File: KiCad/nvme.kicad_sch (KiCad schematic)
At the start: 35 parts, among them J10 Bus_M.2_Socket_M, J11 Bus_M.2_Socket_M, J12 Bus_M.2_Socket_M, J13 Bus_M.2_Socket_M, J14 Bus_M.2_Socket_M

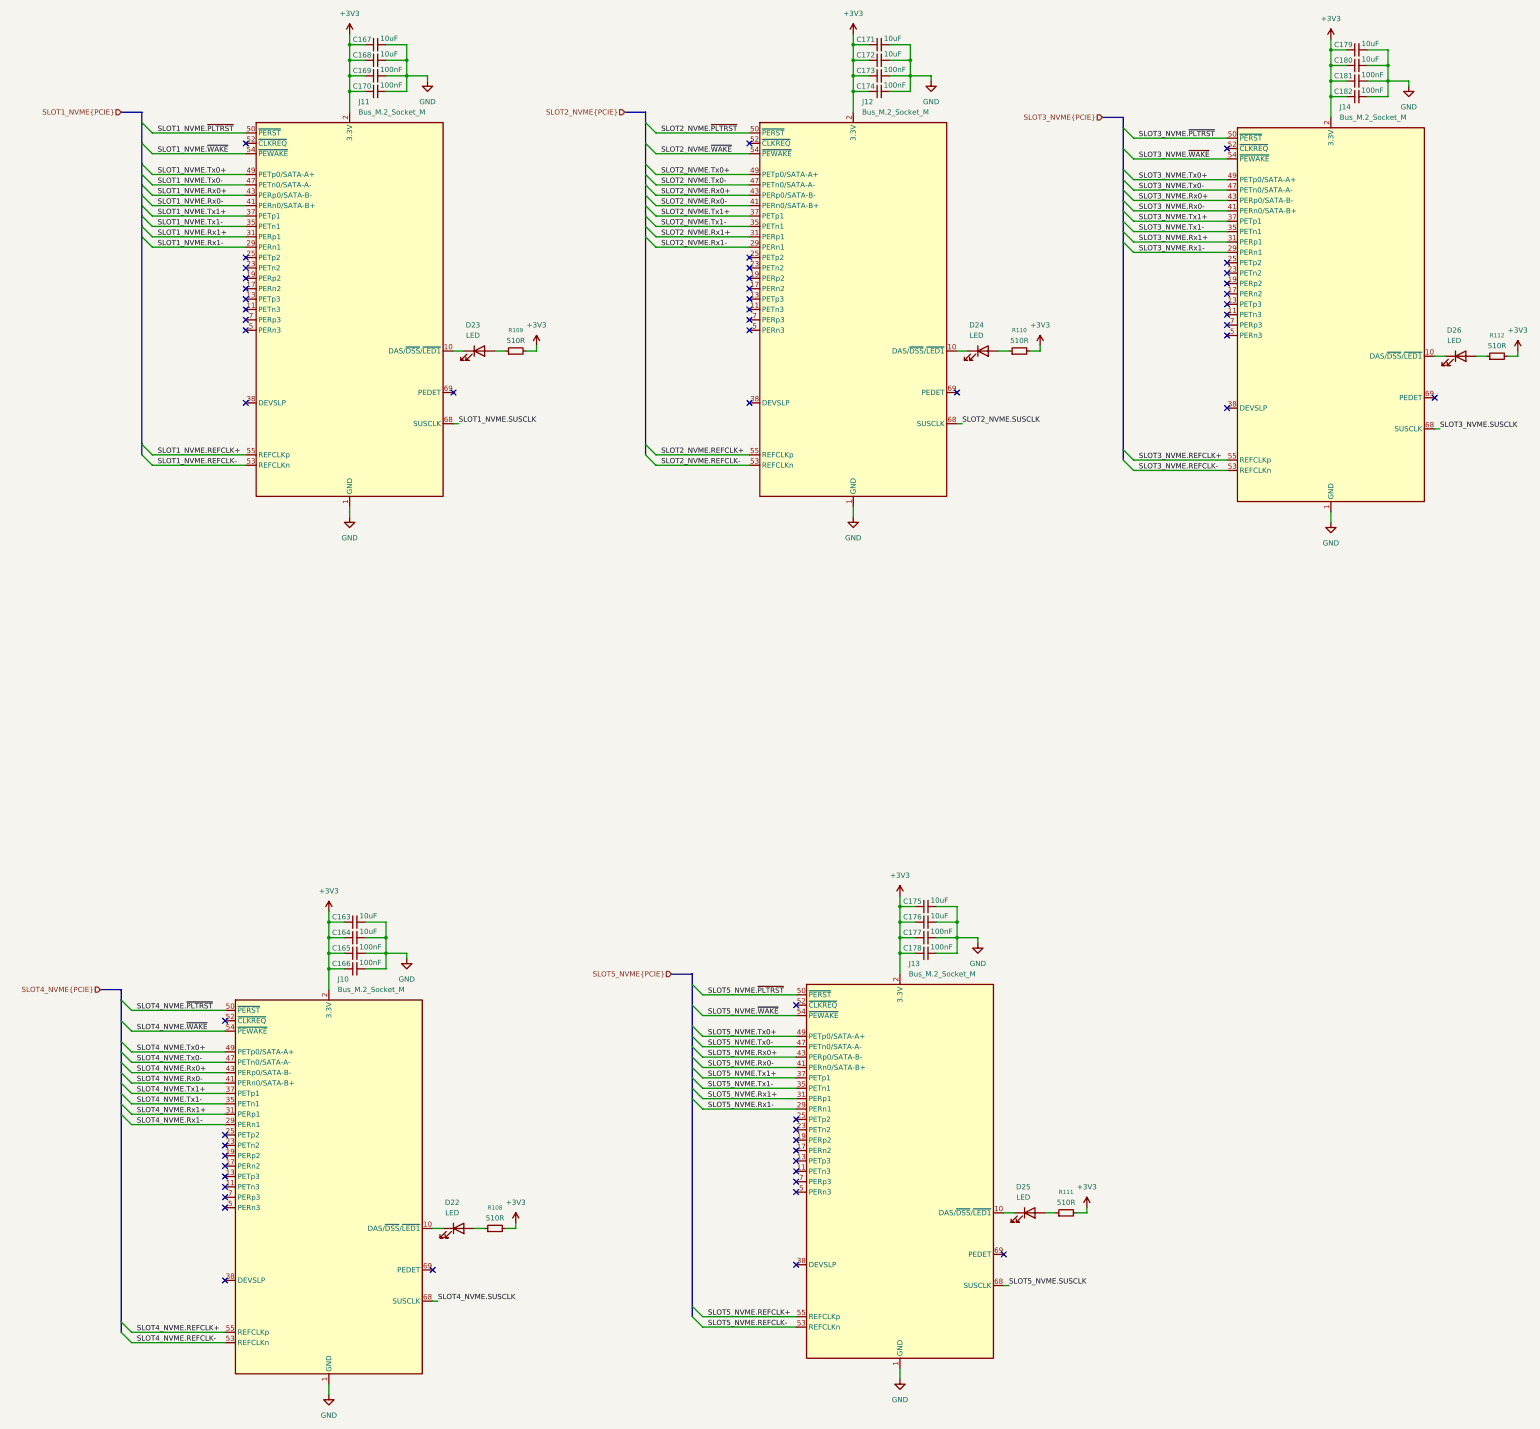
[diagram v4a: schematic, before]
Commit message: Lots of tiny capacitors
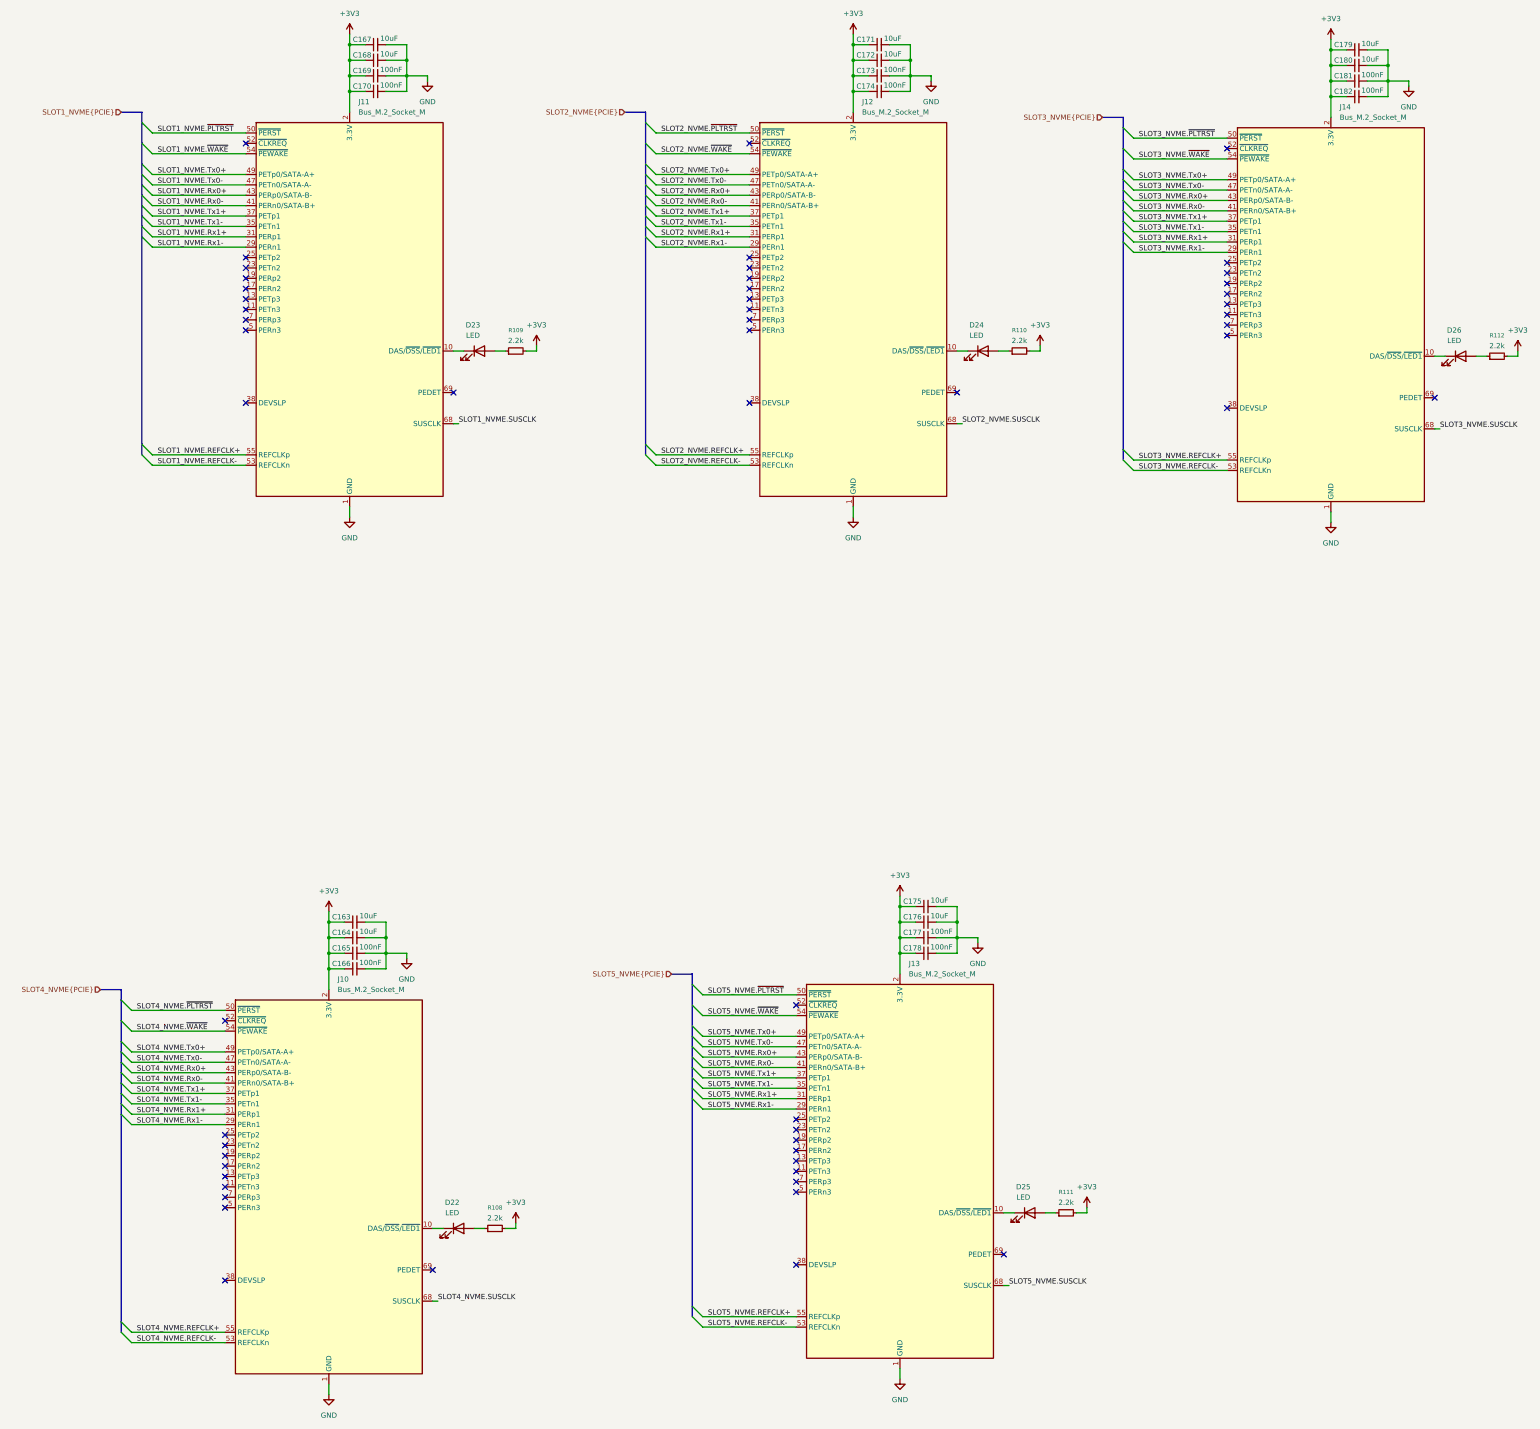
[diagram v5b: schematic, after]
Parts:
- C165, C166, C169, C170, C173, C174, C177, C178, C181, C182: footprint Capacitor_SMD:C_0603_1608Metric -> Capacitor_SMD:C_0402_1005Metric
- R108, R109, R110, R111, R112: value 510R -> 2.2k; footprint (none) -> Resistor_SMD:R_0402_1005Metric
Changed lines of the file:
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@@
 			)
 		)
-		(property "Footprint" "Capacitor_SMD:C_0603_1608Metric"
+		(property "Footprint" "Capacitor_SMD:C_0402_1005Metric"
 			(at 298.45 259.08 0)
 			(effects
@@
 			)
 		)
-		(property "Footprint" "Capacitor_SMD:C_0603_1608Metric"
+		(property "Footprint" "Capacitor_SMD:C_0402_1005Metric"
 			(at 158.75 259.08 0)
 			(effects
@@
 			)
 		)
-		(property "Footprint" "Capacitor_SMD:C_0603_1608Metric"
+		(property "Footprint" "Capacitor_SMD:C_0402_1005Metric"
 			(at 287.02 48.26 0)
 			(effects
@@
 			)
 		)
-		(property "Value" "510R"
+		(property "Value" "2.2k"
 			(at 198.12 109.22 90)
 			(effects
@@
 			)
 		)
-		(property "Footprint" ""
+		(property "Footprint" "Resistor_SMD:R_0402_1005Metric"
 			(at 198.12 111.76 0)
 			(effects
@@
 			)
 		)
-		(property "Value" "510R"
+		(property "Value" "2.2k"
 			(at 193.04 323.85 90)
 			(effects
@@
 			)
 		)
-		(property "Footprint" ""
+		(property "Footprint" "Resistor_SMD:R_0402_1005Metric"
 			(at 193.04 326.39 0)
 			(effects
@@
 			)
 		)
-		(property "Footprint" "Capacitor_SMD:C_0603_1608Metric"
+		(property "Footprint" "Capacitor_SMD:C_0402_1005Metric"
 			(at 163.83 48.26 0)
 			(effects
@@
 			)
 		)
-		(property "Value" "510R"
+		(property "Value" "2.2k"
 			(at 321.31 109.22 90)
 			(effects
@@
 			)
 		)
-		(property "Footprint" ""
+		(property "Footprint" "Resistor_SMD:R_0402_1005Metric"
 			(at 321.31 111.76 0)
 			(effects
@@
 			)
 		)
-		(property "Footprint" "Capacitor_SMD:C_0603_1608Metric"
+		(property "Footprint" "Capacitor_SMD:C_0402_1005Metric"
 			(at 298.45 255.27 0)
 			(effects
@@
 			)
 		)
-		(property "Footprint" "Capacitor_SMD:C_0603_1608Metric"
+		(property "Footprint" "Capacitor_SMD:C_0402_1005Metric"
 			(at 163.83 44.45 0)
 			(effects
@@
 			)
 		)
-		(property "Footprint" "Capacitor_SMD:C_0603_1608Metric"
+		(property "Footprint" "Capacitor_SMD:C_0402_1005Metric"
 			(at 287.02 44.45 0)
 			(effects
@@
 			)
 		)
-		(property "Value" "510R"
+		(property "Value" "2.2k"
 			(at 438.15 110.49 90)
 			(effects
@@
 			)
 		)
-		(property "Footprint" ""
+		(property "Footprint" "Resistor_SMD:R_0402_1005Metric"
 			(at 438.15 113.03 0)
 			(effects
@@
 			)
 		)
-		(property "Footprint" "Capacitor_SMD:C_0603_1608Metric"
+		(property "Footprint" "Capacitor_SMD:C_0402_1005Metric"
 			(at 403.86 49.53 0)
 			(effects
@@
 			)
 		)
-		(property "Footprint" "Capacitor_SMD:C_0603_1608Metric"
+		(property "Footprint" "Capacitor_SMD:C_0402_1005Metric"
 			(at 403.86 45.72 0)
 			(effects
@@
 			)
 		)
-		(property "Value" "510R"
+		(property "Value" "2.2k"
 			(at 332.74 320.04 90)
 			(effects
@@
 			)
 		)
-		(property "Footprint" ""
+		(property "Footprint" "Resistor_SMD:R_0402_1005Metric"
 			(at 332.74 322.58 0)
 			(effects
@@
 			)
 		)
-		(property "Footprint" "Capacitor_SMD:C_0603_1608Metric"
+		(property "Footprint" "Capacitor_SMD:C_0402_1005Metric"
 			(at 158.75 262.89 0)
 			(effects

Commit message: Add most passive component footprints
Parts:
- D22, D23, D24, D25, D26: footprint (none) -> LED_SMD:LED_0603_1608Metric
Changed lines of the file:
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@@
 			)
 		)
-		(property "Footprint" ""
+		(property "Footprint" "LED_SMD:LED_0603_1608Metric"
 			(at 429.26 113.03 0)
 			(effects
@@
 			)
 		)
-		(property "Footprint" ""
+		(property "Footprint" "LED_SMD:LED_0603_1608Metric"
 			(at 184.15 326.39 0)
 			(effects
@@
 			)
 		)
-		(property "Footprint" ""
+		(property "Footprint" "LED_SMD:LED_0603_1608Metric"
 			(at 323.85 322.58 0)
 			(effects
@@
 			)
 		)
-		(property "Footprint" ""
+		(property "Footprint" "LED_SMD:LED_0603_1608Metric"
 			(at 312.42 111.76 0)
 			(effects
@@
 			)
 		)
-		(property "Footprint" ""
+		(property "Footprint" "LED_SMD:LED_0603_1608Metric"
 			(at 189.23 111.76 0)
 			(effects

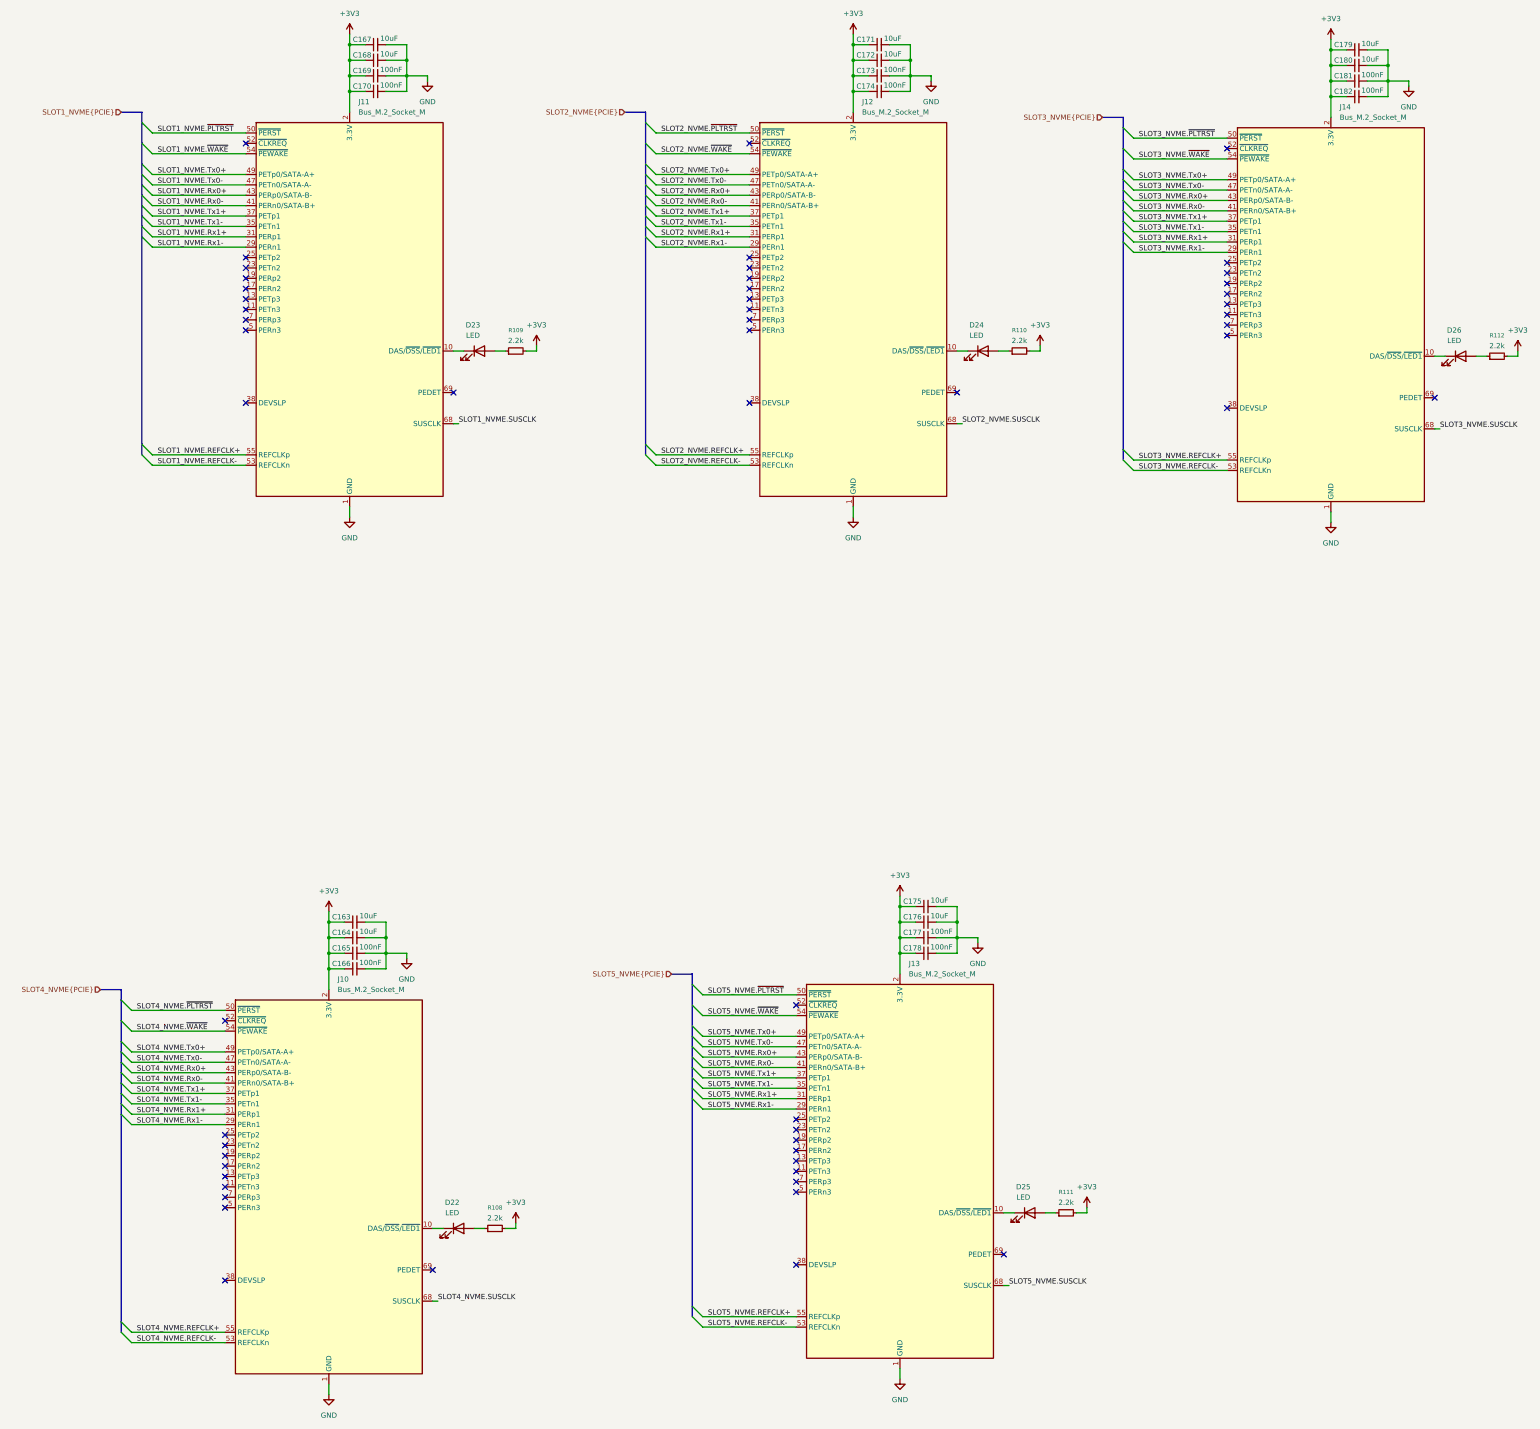
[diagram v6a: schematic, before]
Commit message: Add m.2 slot footprints
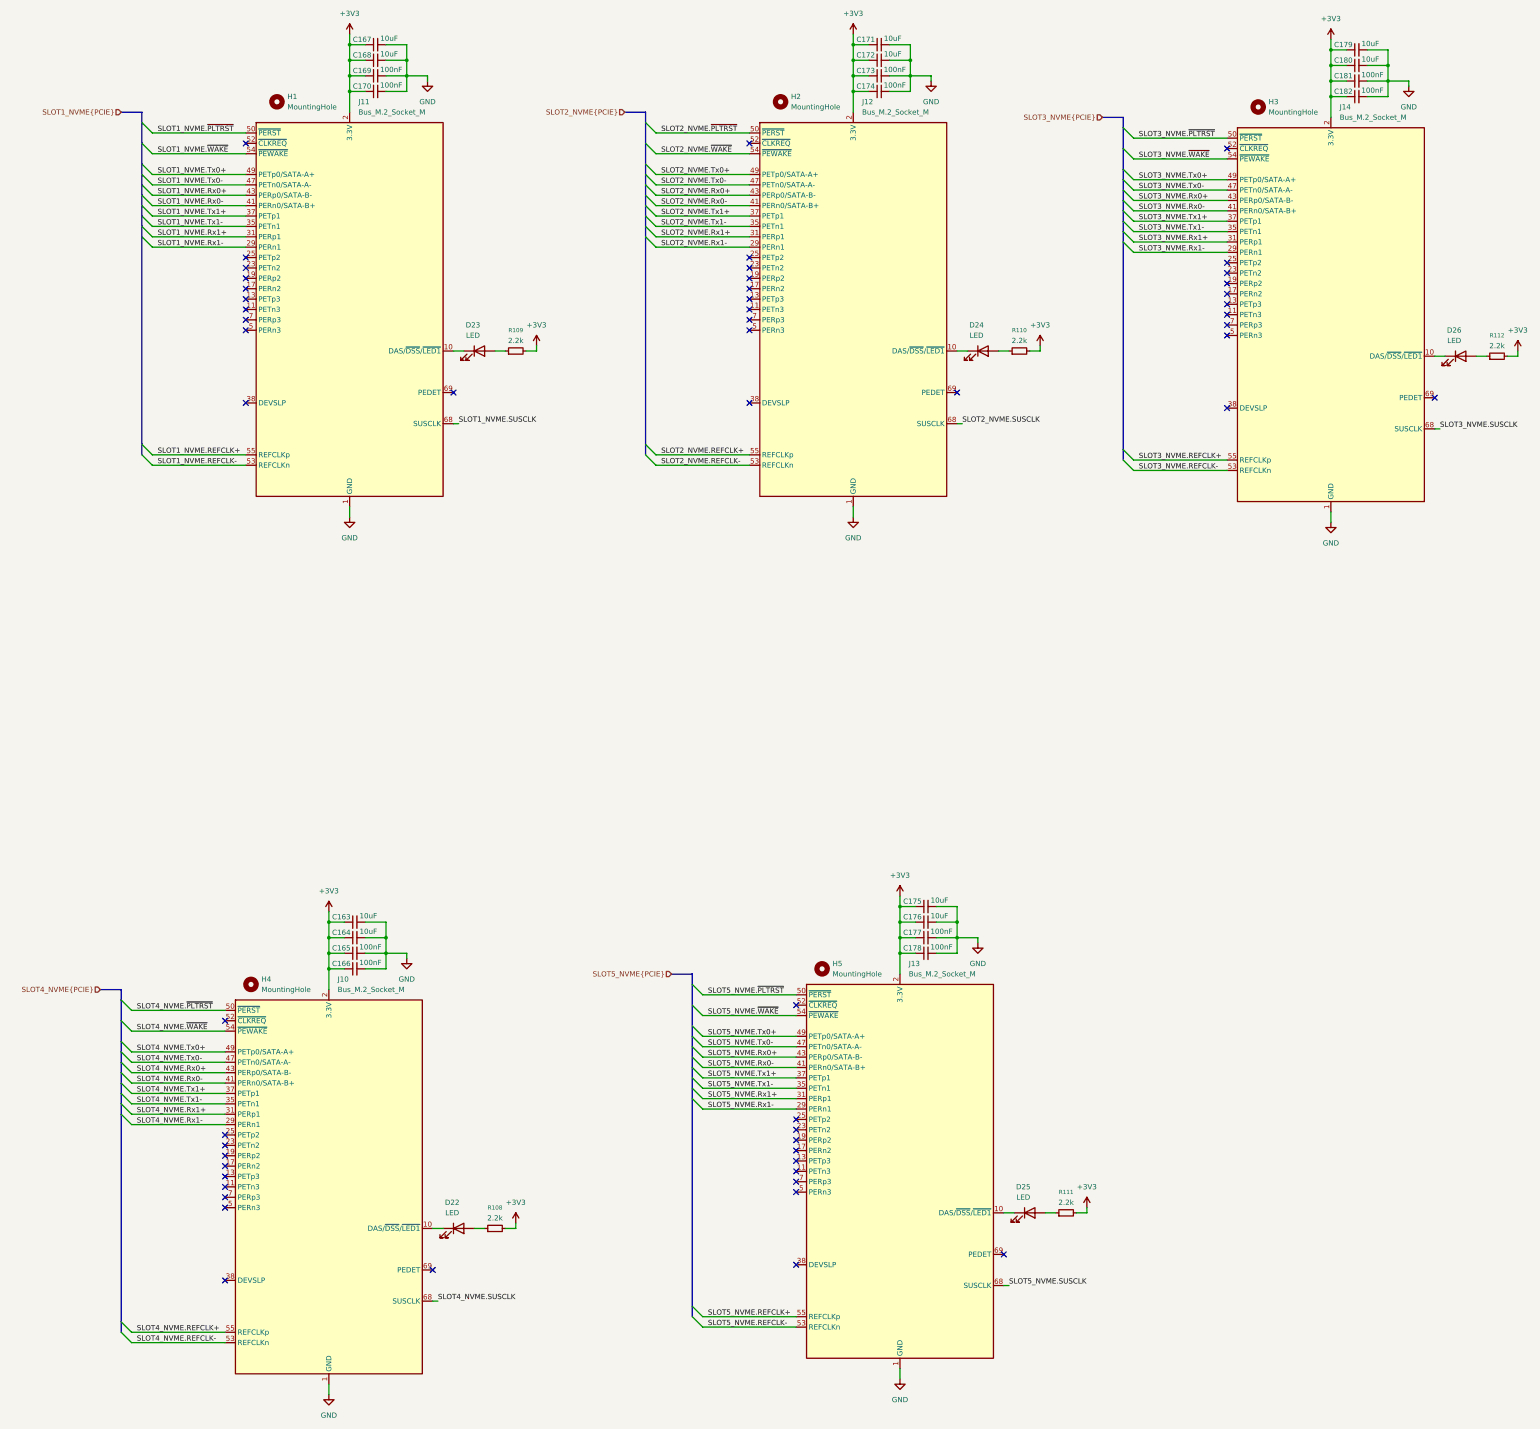
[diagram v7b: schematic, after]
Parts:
- added H1, H2, H3, H4, H5: MountingHole, symbol Mechanical:MountingHole
- J10, J11, J12, J13, J14: footprint (none) -> EasyEDA2KiCAD:CONN-SMD_AS0BC21-S30BM-7H
